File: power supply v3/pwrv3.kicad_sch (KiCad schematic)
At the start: 46 parts, among them IC2 LM25145RGYR, IC3 LMR50410YQDBVRQ1, J1 1.5 mm, J3 1933189, J4 Conn_01x04_Pin 1.27mm, Q1 35A, 30V, Q2 35A Id, 30V Vds

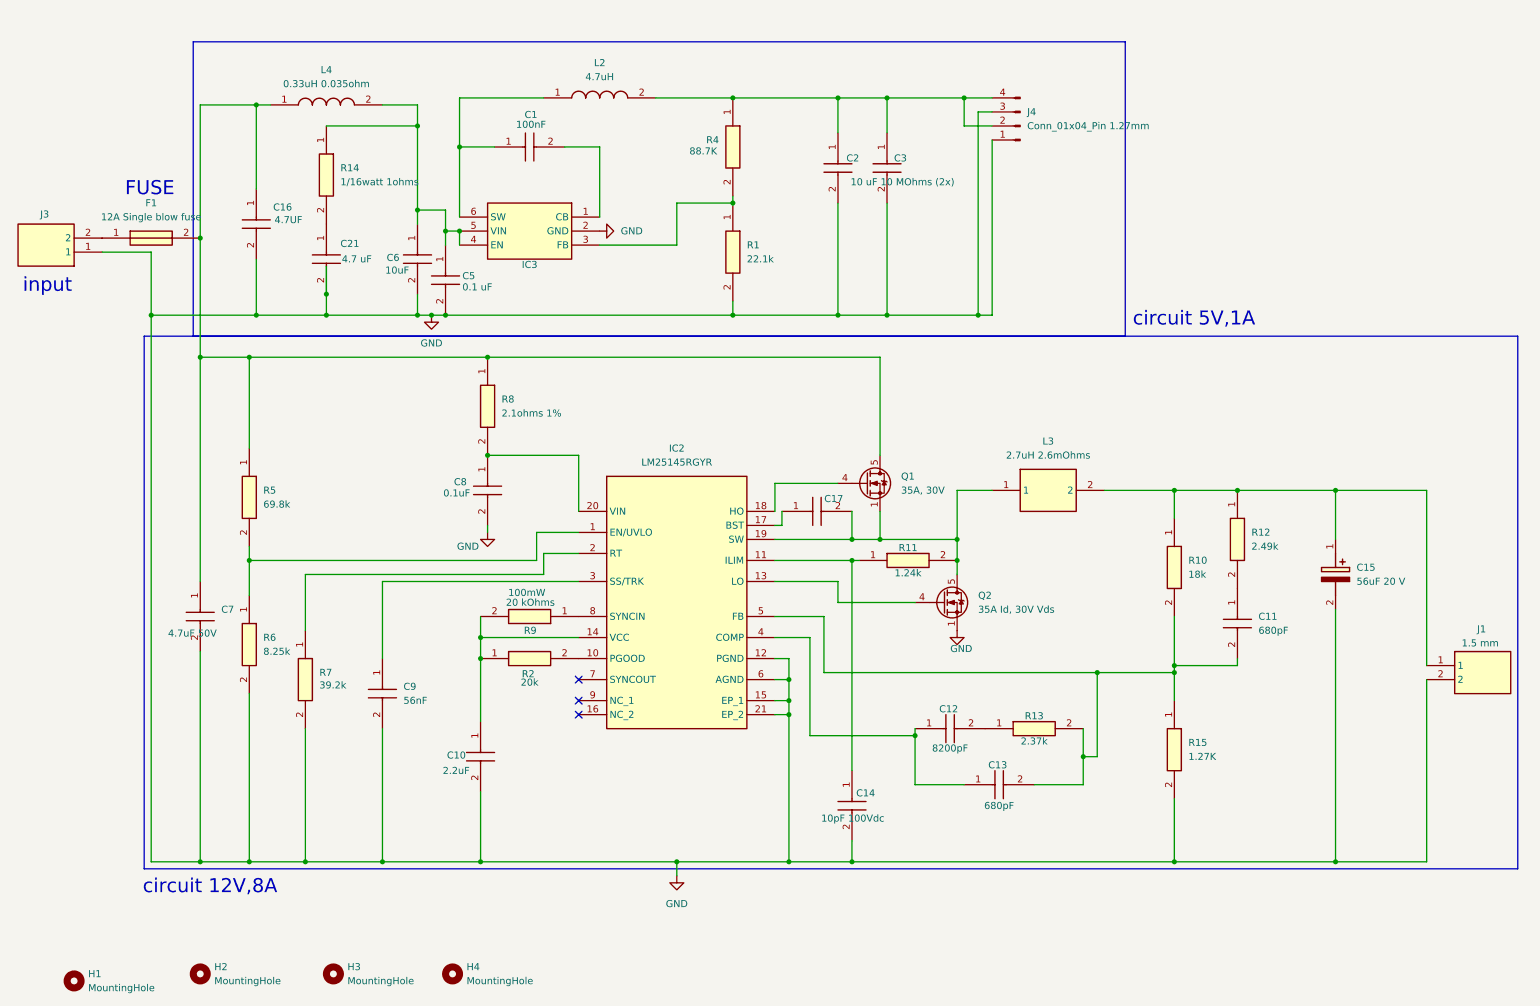
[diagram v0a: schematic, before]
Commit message: add the LED to electronics schematics
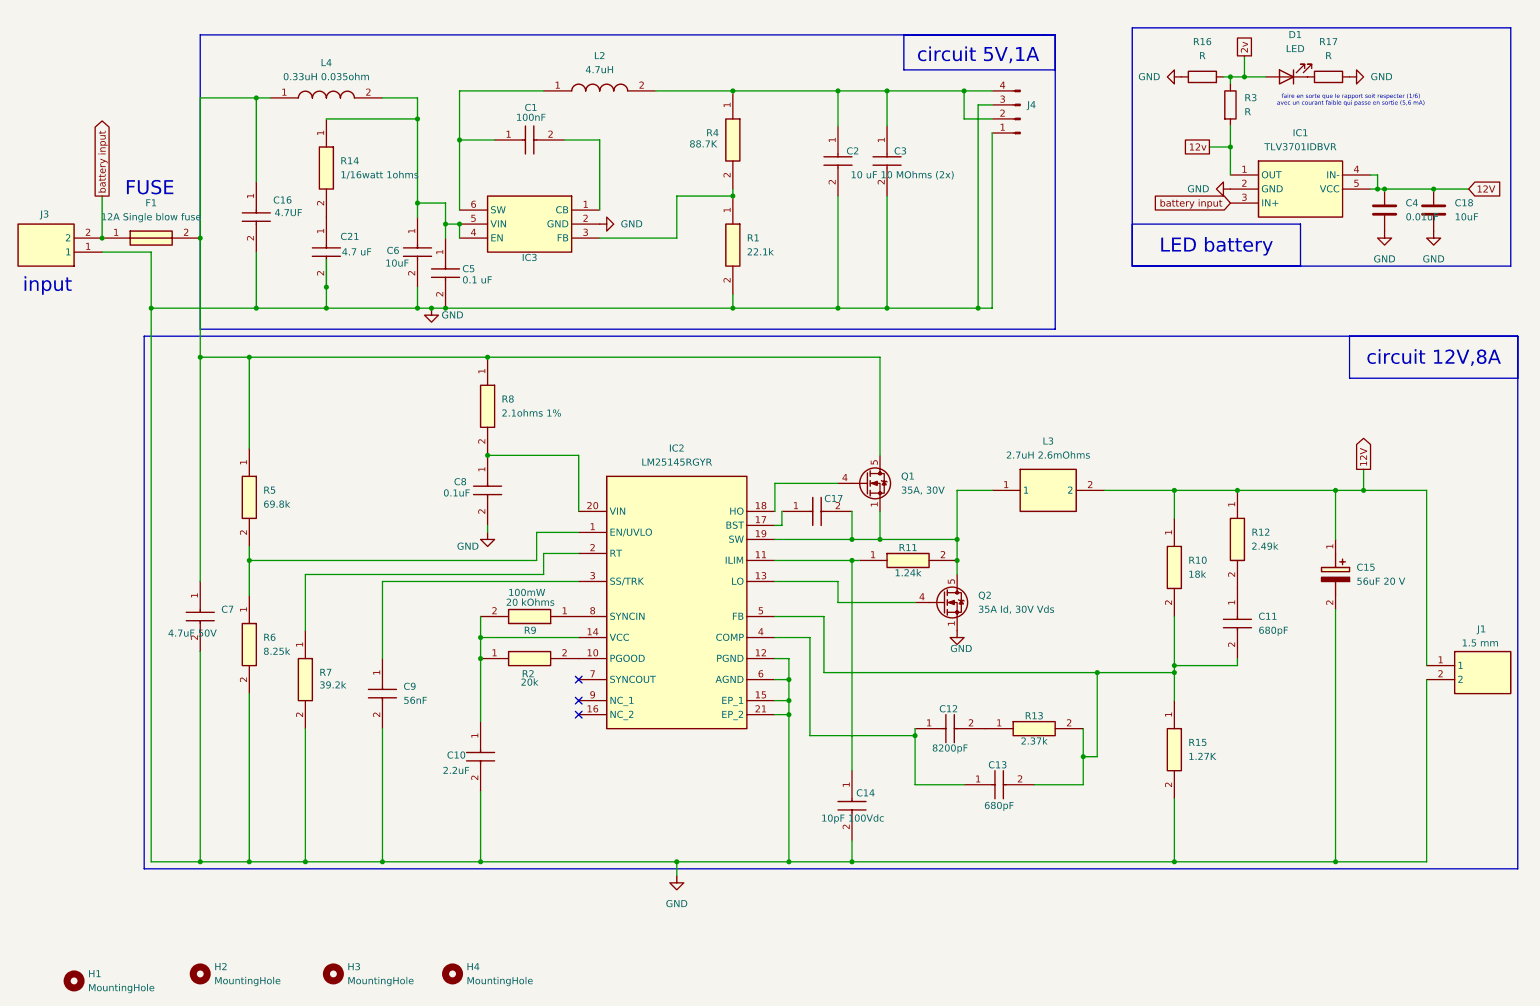
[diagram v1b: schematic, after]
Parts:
- added C18: 10uF, symbol Device:C
- added C4: 0.01uF, symbol Device:C
- added D1: LED, symbol Device:LED
- added IC1: TLV3701IDBVR, SOT95P280X145-5N, symbol TLV3701IDBVR:TLV3701IDBVR
- added R16, R17, R3: R, symbol Device:R
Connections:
- net GND: now also C18.2, C4.2, IC1.2 (GND), R16.1, R17.2
- net 12V: now reaches C15.1 (+), J1.1, L3.2, R10.1, R12.1
- net 12V: now also C18.1, C4.1, IC1.4 (IN-), IC1.5 (VCC)
- net battery input: now reaches F1.1, J3.2
- net battery input: now also IC1.3 (IN+)
- new net: D1.1 (K), R17.1
- new net 12v: IC1.1 (OUT), R3.2
- new net 2v: D1.2 (A), R16.2, R3.1
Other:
- note added: "LED battery"
- note added: "faire en sorte que le rapport soit respecter (1/6) avec un courant faible qui passe en sortie (5,6 mA)"
- company: (none) -> N-Pulse
- title: (none) -> Power Board N-pulse V3
- moved on the sheet: C1, C16, C2, C21, C3, C5, C6, IC3, J4, L2, L4, R1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

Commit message: new layout and pin moved
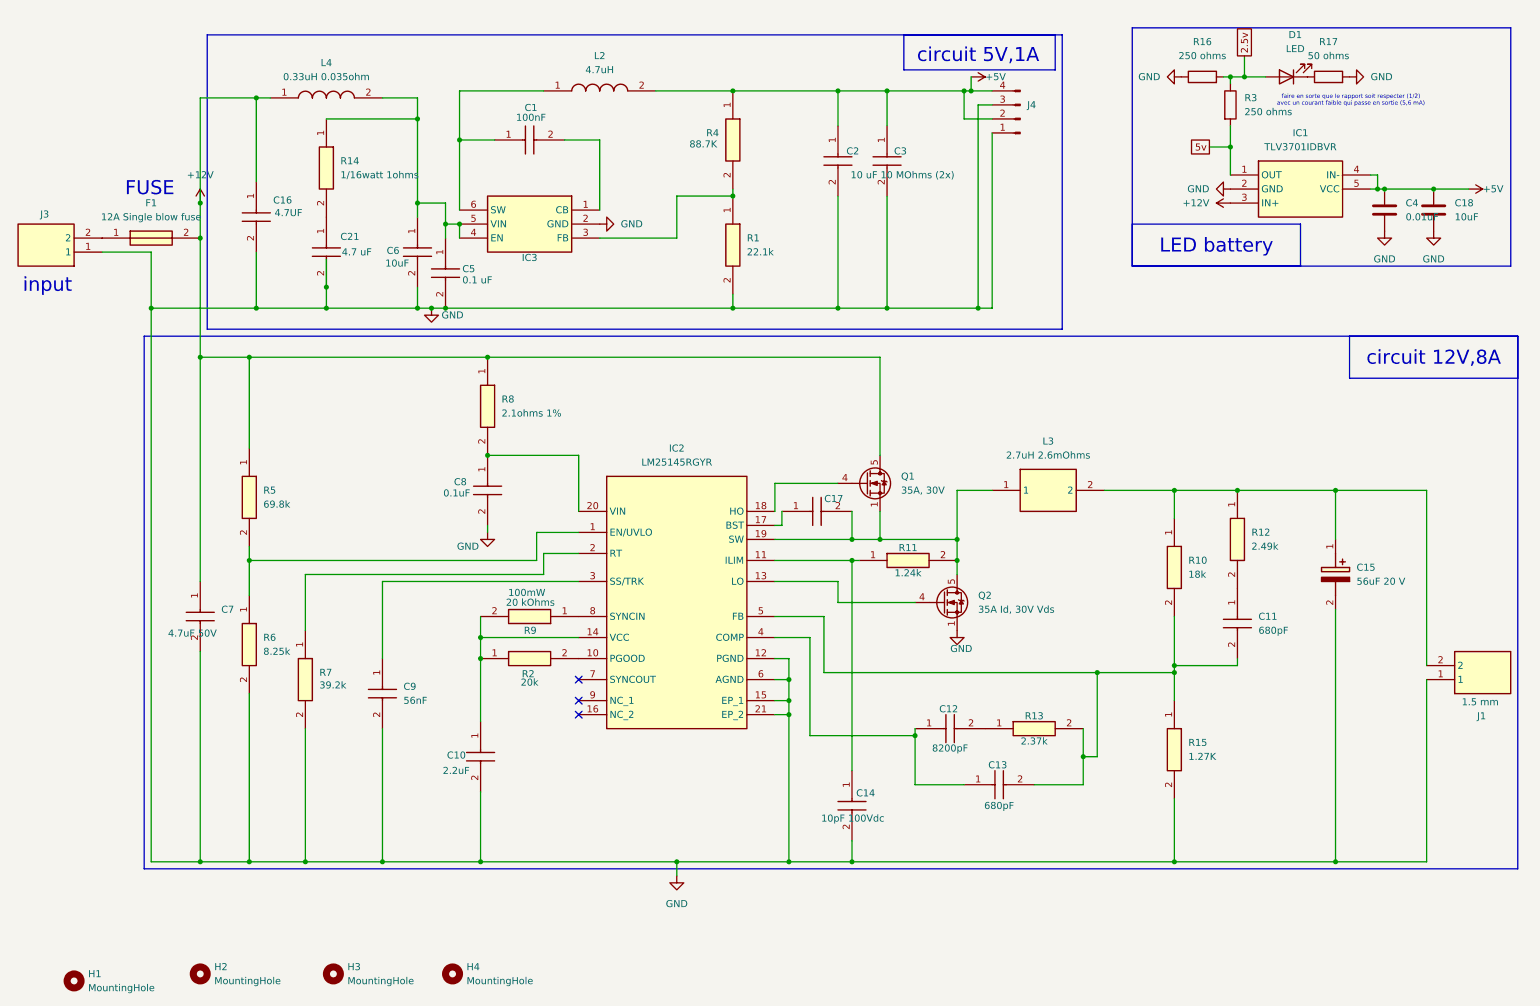
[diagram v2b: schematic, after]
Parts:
- C1, C10, C11, C12, C13, C9: footprint CAPC1005X55N -> Capacitor_SMD:C_0402_1005Metric
- C14, C8: footprint CAPC1608X90N -> Capacitor_SMD:C_0603_1608Metric
- C16: footprint CAPC3216X180N -> Capacitor_SMD:C_1206_3216Metric
- C17: footprint GCM155 -> Capacitor_SMD:C_0402_1005Metric
- C18: footprint (none) -> Capacitor_SMD:C_0603_1608Metric
- C2, C3: footprint C0805 -> Capacitor_SMD:C_0805_2012Metric
- C21: footprint CAPC3225X200N -> Capacitor_SMD:C_1210_3225Metric
- C4: footprint (none) -> Capacitor_SMD:C_1206_3216Metric
- C5: footprint GRM18x -> Capacitor_SMD:C_0603_1608Metric
- C6: footprint CAPC1608X80N -> Capacitor_SMD:C_0603_1608Metric
- C7: footprint CAPC3225X270N -> Capacitor_SMD:C_1210_3225Metric
- D1: footprint (none) -> Diode_SMD:D_1206_3216Metric
- F1: footprint FUSC3216X117N -> Fuse:Fuse_1206_3216Metric
- J4: footprint Connector_PinHeader_1.27mm:PinHeader_1x04_P1.27mm_Vertical -> Connector_PinHeader_2.54mm:PinHeader_1x04_P2.54mm_Vertical
- L4: footprint INDPM3225X240N -> Inductor_SMD:L_1210_3225Metric
- R1, R11, R12, R13, R14, R15, R4, R5, R7: footprint RESC1005X40N -> Resistor_SMD:R_0402_1005Metric
- R10, R2, R9: footprint RESC1608X55N -> Resistor_SMD:R_0603_1608Metric
- R16, R3: value R -> 250 ohms; footprint (none) -> Resistor_SMD:R_0603_1608Metric
- R17: value R -> 50 ohms; footprint (none) -> Resistor_SMD:R_0402_1005Metric
- R6: footprint RESC1608X50N -> Resistor_SMD:R_0201_0603Metric
- R8: footprint RESC1608X50N -> Resistor_SMD:R_0603_1608Metric
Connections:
- net GND: now also J1.1; no longer J1.2
- net +5V: now reaches C2.1, C3.1, J4.2 (Pin_2), J4.4 (Pin_4), L2.2, R4.1
- net +5V: now also C18.1, C4.1, IC1.4 (IN-), IC1.5 (VCC)
- net +12V: now reaches C16.1, C7.1, F1.2, L4.1, Q1.5 (D), R5.1, R8.1
- net +12V: now also IC1.3 (IN+)
- removed net 12V: C15.1 (+), C18.1, C4.1, IC1.4 (IN-), IC1.5 (VCC), J1.1, L3.2, R10.1, R12.1
- net 12v renamed 5v
- net 2v renamed 2.5v
- net battery input: no longer names the net of F1.1, J3.2
- net battery input: no longer IC1.3 (IN+)
- new net: C15.1 (+), J1.2, L3.2, R10.1, R12.1
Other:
- note added: "faire en sorte que le rapport soit respecter (1/2) avec un courant faible qui passe en sortie (5,6 mA)"
- note removed: "faire en sorte que le rapport soit respecter (1/6) avec un courant faible qui passe en sortie (5,6 mA)"

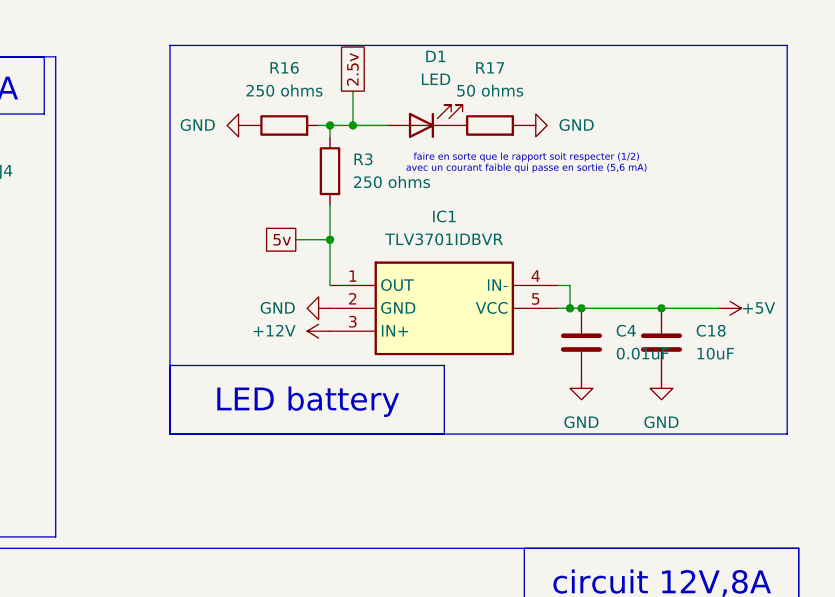
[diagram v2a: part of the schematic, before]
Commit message: entree comparateur 5V
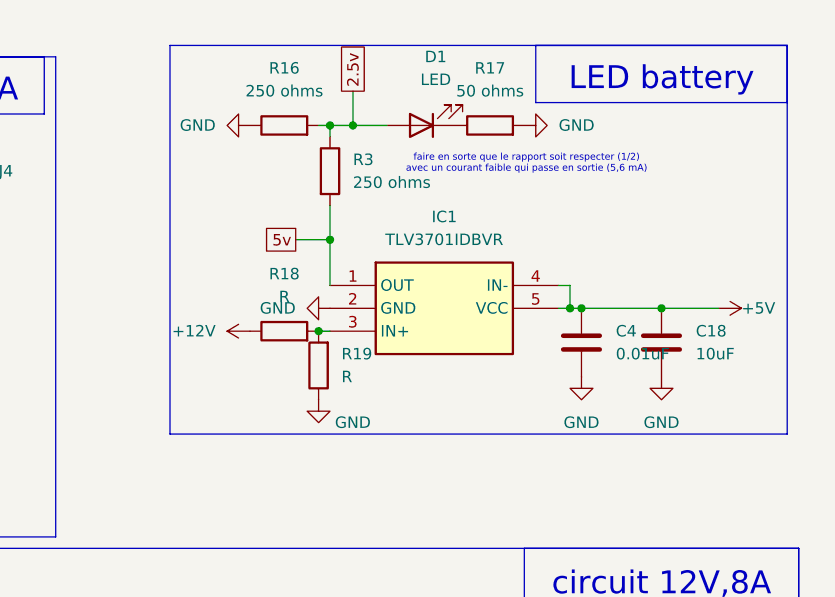
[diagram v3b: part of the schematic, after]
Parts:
- added R18, R19: R, Resistor_SMD:R_0402_1005Metric, symbol Device:R
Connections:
- net +12V: now also R18.1; no longer IC1.3 (IN+)
- net GND: now also R19.1
- new net: IC1.3 (IN+), R18.2, R19.2
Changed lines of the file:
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@@
 	)
 	(rectangle
-		(start 214.63 48.26)
-		(end 245.11 55.88)
+		(start 255.27 12.7)
+		(end 283.21 19.05)
 		(stroke
 			(width 0)
@@
 	(text "LED battery"
 		(exclude_from_sim no)
-		(at 229.87 52.324 0)
+		(at 269.24 16.51 0)
 		(effects
 			(font
@@
 	)
 	(junction
+		(at 231.14 44.45)
+		(diameter 0)
+		(color 0 0 0 0)
+	)
+	(junction
 		(at 68.58 59.69)
 		(diameter 0)
@@
 	(wire
 		(pts
+			(xy 231.14 44.45) (xy 232.41 44.45)
+		)
+		(stroke
+			(width 0)
+			(type default)
+		)
+	)
+	(wire
+		(pts
 			(xy 251.46 96.52) (xy 267.97 96.52)
 		)
@@
 	)
 	(symbol
+		(lib_id "Device:R")
+		(at 231.14 48.26 180)
+		(unit 1)
+		(exclude_from_sim no)
+		(in_bom yes)
+		(on_board yes)
+		(dnp no)
+		(fields_autoplaced yes)
+		(property "Reference" "R19"
+			(at 233.68 46.9899 0)
+			(effects
+				(font
+					(size 1.27 1.27)
+				)
+				(justify right)
+			)
+		)
+		(property "Value" "R"
+			(at 233.68 49.5299 0)
+			(effects
+				(font
+					(size 1.27 1.27)
+				)
+				(justify right)
+			)
+		)
+		(property "Footprint" "Resistor_SMD:R_0402_1005Metric"
+			(at 232.918 48.26 90)
+			(effects
+				(font
+					(size 1.27 1.27)
+				)
+				(hide yes)
+			)
+		)
+		(property "Datasheet" "~"
+			(at 231.14 48.26 0)
+			(effects
+				(font
+					(size 1.27 1.27)
+				)
+				(hide yes)
+			)
+		)
+		(property "Description" "Resistor"
+			(at 231.14 48.26 0)
+			(effects
+				(font
+					(size 1.27 1.27)
+				)
+				(hide yes)
+			)
+		)
+		(pin "1"
+		)
+		(pin "2"
+		)
+		(instances
+			(project "pwrv3"
+				(path "/227c4948-9b5e-42be-82b5-2619f1ed7477"
+					(reference "R19")
+					(unit 1)
+				)
+			)
+		)
+	)
+	(symbol
 		(lib_id "power:GND")
 		(at 132.08 166.37 0)
@@
 	)
 	(symbol
+		(lib_id "Device:R")
+		(at 227.33 44.45 90)
+		(unit 1)
+		(exclude_from_sim no)
+		(in_bom yes)
+		(on_board yes)
+		(dnp no)
+		(fields_autoplaced yes)
+		(property "Reference" "R18"
+			(at 227.33 38.1 90)
+			(effects
+				(font
+					(size 1.27 1.27)
+				)
+			)
+		)
+		(property "Value" "R"
+			(at 227.33 40.64 90)
+			(effects
+				(font
+					(size 1.27 1.27)
+				)
+			)
+		)
+		(property "Footprint" "Resistor_SMD:R_0402_1005Metric"
+			(at 227.33 46.228 90)
+			(effects
+				(font
+					(size 1.27 1.27)
+				)
+				(hide yes)
+			)
+		)
+		(property "Datasheet" "~"
+			(at 227.33 44.45 0)
+			(effects
+				(font
+					(size 1.27 1.27)
+				)
+				(hide yes)
+			)
+		)
+		(property "Description" "Resistor"
+			(at 227.33 44.45 0)
+			(effects
+				(font
+					(size 1.27 1.27)
+				)
+				(hide yes)
+			)
+		)
+		(pin "1"
+		)
+		(pin "2"
+		)
+		(instances
+			(project ""
+				(path "/227c4948-9b5e-42be-82b5-2619f1ed7477"
+					(reference "R18")
+					(unit 1)
+				)
+			)
+		)
+	)
+	(symbol
 		(lib_id "power:GND")
 		(at 254 21.59 90)
@@
 	(symbol
 		(lib_id "power:+12V")
-		(at 232.41 44.45 90)
+		(at 223.52 44.45 90)
 		(unit 1)
 		(exclude_from_sim no)
@@
 		(fields_autoplaced yes)
 		(property "Reference" "#PWR013"
-			(at 236.22 44.45 0)
+			(at 227.33 44.45 0)
 			(effects
 				(font
@@
 		)
 		(property "Value" "+12V"
-			(at 228.6 44.4499 90)
+			(at 219.71 44.4499 90)
 			(effects
 				(font
@@
 		)
 		(property "Footprint" ""
-			(at 232.41 44.45 0)
+			(at 223.52 44.45 0)
 			(effects
 				(font
@@
 		)
 		(property "Datasheet" ""
-			(at 232.41 44.45 0)
+			(at 223.52 44.45 0)
 			(effects
 				(font
@@
 		)
 		(property "Description" "Power symbol creates a global label with name \"+12V\""
-			(at 232.41 44.45 0)
+			(at 223.52 44.45 0)
 			(effects
 				(font
@@
 					(unit 1)
 				)
+			)
+		)
+	)
+	(symbol
+		(lib_id "power:GND")
+		(at 231.14 52.07 0)
+		(unit 1)
+		(exclude_from_sim no)
+		(in_bom yes)
+		(on_board yes)
+		(dnp no)
+		(property "Reference" "#PWR015"
+			(at 231.14 58.42 0)
+			(effects
+				(font
+					(size 1.27 1.27)
+				)
+				(hide yes)
+			)
+		)
+		(property "Value" "GND"
+			(at 234.95 54.61 0)
+			(effects
+				(font
+					(size 1.27 1.27)
+				)
+			)
+		)
+		(property "Footprint" ""
+			(at 231.14 52.07 0)
+			(effects
+				(font
+					(size 1.27 1.27)
+				)
+				(hide yes)
+			)
+		)
+		(property "Datasheet" ""
+			(at 231.14 52.07 0)
+			(effects
+				(font
+					(size 1.27 1.27)
+				)
+				(hide yes)
+			)
+		)
+		(property "Description" "Power symbol creates a global label with name \"GND\" , ground"
+			(at 231.14 52.07 0)
+			(effects
+				(font
+					(size 1.27 1.27)
+				)
+				(hide yes)
+			)
+		)
+		(pin "1"
+		)
+		(instances
+			(project "pwrv3"
+				(path "/227c4948-9b5e-42be-82b5-2619f1ed7477"
+					(reference "#PWR015")
+					(unit 1)
+				)
